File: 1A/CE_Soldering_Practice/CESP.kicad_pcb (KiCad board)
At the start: 2 copper layers, 49.8 x 25.9 mm, 44 parts, among them Q1 BC847, Q2 BC847, Q3 BC847, Q4 BC847, U1 7555, U2 74HC04, U3 BA2904, U4 BA2904

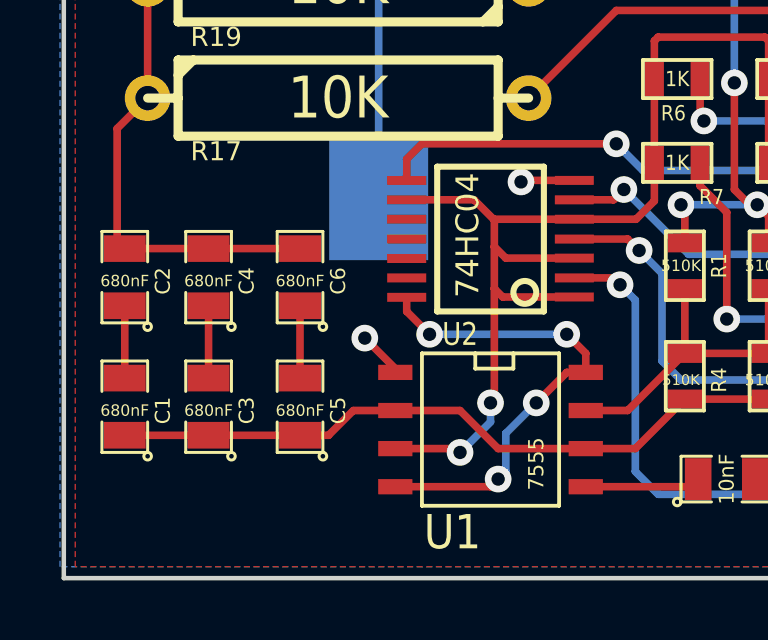
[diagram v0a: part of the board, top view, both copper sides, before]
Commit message: Add missing VCC trace
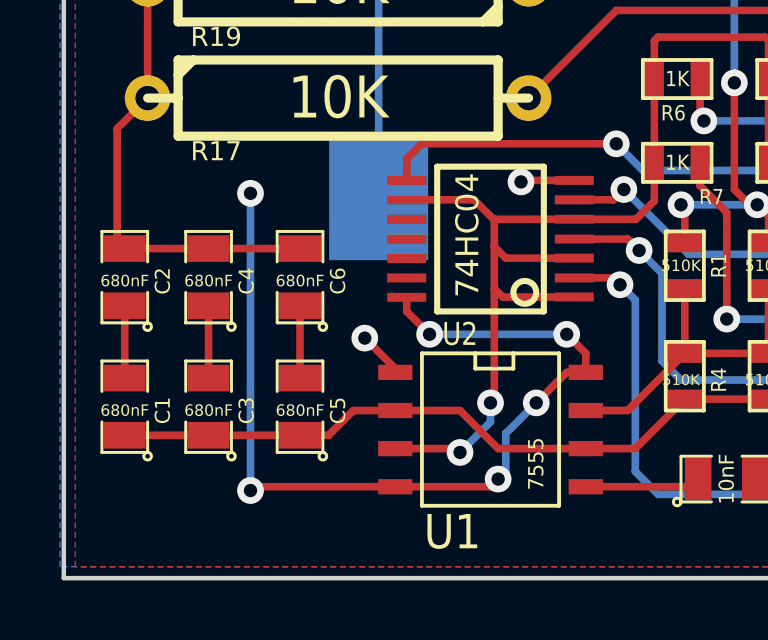
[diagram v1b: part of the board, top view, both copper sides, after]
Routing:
- net VCC: track 58.0 -> 72.8 mm, vias 8 -> 10
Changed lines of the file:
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@@
     (thickness 1.6)
     (drawings 14)
-    (tracks 266)
+    (tracks 271)
     (zones 0)
     (modules 44)
@@
   (segment (start 181.61 134.62) (end 181.61 127.254) (width 0.254) (layer F.Cu) (net 31))
   (segment (start 182.8165 135.8265) (end 181.61 134.62) (width 0.254) (layer F.Cu) (net 31))
+  (segment (start 168.021 137.668) (end 163.322 137.668) (width 0.254) (layer F.Cu) (net 32))
+  (via (at 163.195 127.889) (size 0.889) (layers F.Cu B.Cu) (net 32))
+  (segment (start 163.195 137.795) (end 163.195 127.889) (width 0.254) (layer B.Cu) (net 32))
+  (via (at 163.195 137.795) (size 0.889) (layers F.Cu B.Cu) (net 32))
+  (segment (start 163.322 137.668) (end 163.195 137.795) (width 0.254) (layer F.Cu) (net 32))
   (segment (start 204.597 127.127) (end 204.597 125.349) (width 0.254) (layer F.Cu) (net 32))
   (segment (start 204.597 125.349) (end 203.708 124.46) (width 0.254) (layer F.Cu) (net 32))
